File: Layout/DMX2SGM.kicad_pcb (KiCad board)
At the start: 2 copper layers, 66.4 x 90.9 mm, 38 parts, among them J1 AVR-ISP-6, J2 Conn_01x03, J3 Conn_01x03, J4 Conn_01x03, J5 Conn_01x03, SW1 BD09AV, U1 ATtiny1634, U2 485, U3 6N137, U4 REE-0505S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

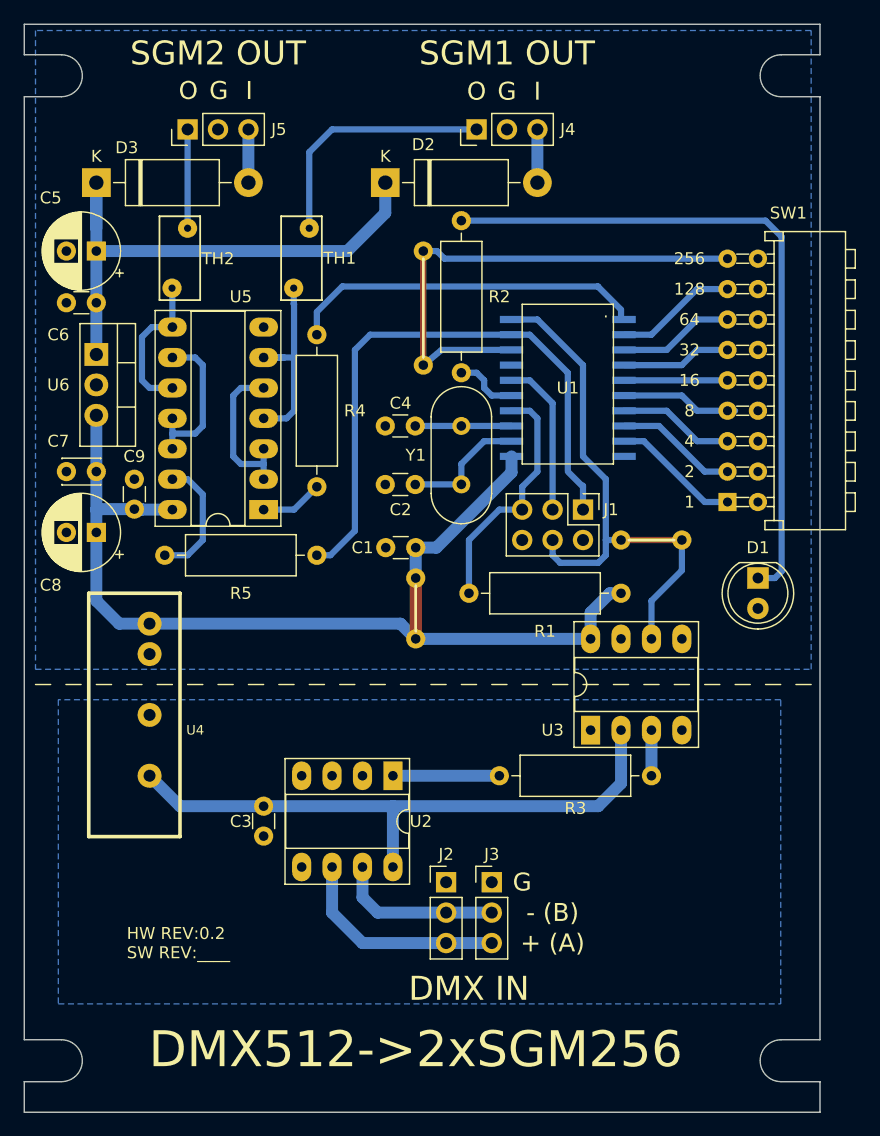
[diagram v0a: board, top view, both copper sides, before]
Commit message: Bugfixes & Cleanup
Code cleanup, Fixing a few bugs, General code optimations
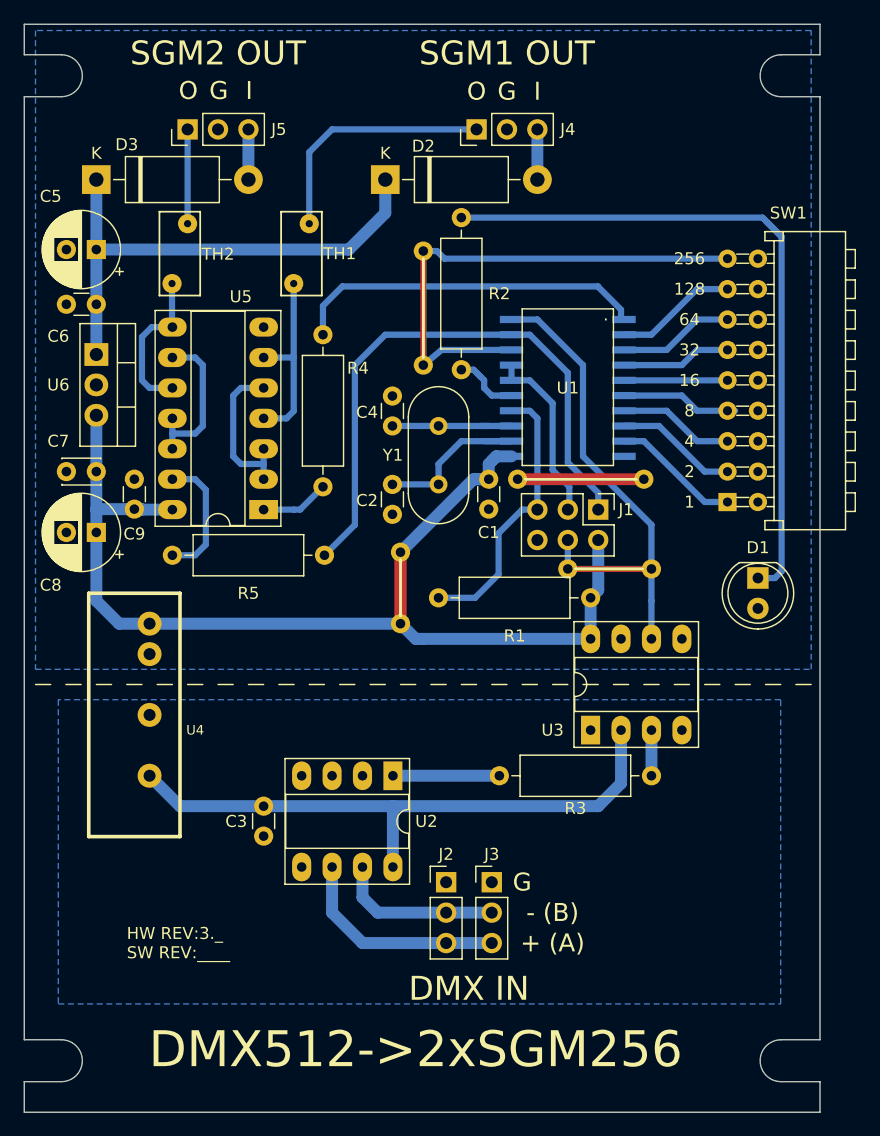
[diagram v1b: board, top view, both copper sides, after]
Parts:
- removed the REF** at (92.7, 101.0)
- removed the REF** at (109.9, 92.7)
- removed the REF** at (114.9, 92.7)
- added REF**: SolderWirePad_single_0-8mmDrill, Wire_Pads:SolderWirePad_single_0-8mmDrill, F.Cu at (101.2, 87.6)
- added REF**: SolderWirePad_single_0-8mmDrill, Wire_Pads:SolderWirePad_single_0-8mmDrill, F.Cu at (111.8, 87.6)
- added REF**: SolderWirePad_single_0-8mmDrill, Wire_Pads:SolderWirePad_single_0-8mmDrill, F.Cu at (91.4, 99.7)
- added REF**: SolderWirePad_single_0-8mmDrill, Wire_Pads:SolderWirePad_single_0-8mmDrill, F.Cu at (105.4, 95.1)
- added REF**: SolderWirePad_single_0-8mmDrill, Wire_Pads:SolderWirePad_single_0-8mmDrill, F.Cu at (112.4, 95.1)
- moved C1 8.36 mm to (98.8, 87.6), turned to 270 degrees
- moved R1 2.57 mm to (94.6, 97.5)
- moved C2 2.56 mm to (90.8, 90.6), turned to 90 degrees
- moved REF** 2.50 mm to (91.4, 93.7)
- moved C4 1.91 mm to (90.8, 83.2), turned to 90 degrees
- moved Y1 1.91 mm to (94.6, 83.2)
- moved J1 1.27 mm to (108.0, 90.2)
- moved R5 0.64 mm to (72.4, 94.0)
- moved R4 0.51 mm to (85.0, 88.3)
- moved TH1 0.38 mm to (83.8, 66.3)
- moved TH2 0.38 mm to (73.7, 66.3)
- moved D2 0.25 mm to (90.2, 62.6)
- moved D3 0.25 mm to (66.0, 62.6)
- moved R2 0.25 mm to (96.5, 65.8)
- moved C6 0.13 mm to (66.0, 73.0)
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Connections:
- J1 pad 2: (no net) -> +5VD
- U1 pad 17: (no net) -> ICSP_SCL
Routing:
- net GNDD: track 0.00 -> 10.5 mm
- net +5VD: track 89.2 -> 94.5 mm
- net DMX: track 47.4 -> 42.2 mm
- net Net-(C2-Pad2): track 9.90 -> 14.1 mm
- net +VSW: track 45.8 -> 42.8 mm
- net RESET: track 20.5 -> 23.4 mm
- net Net-(C4-Pad1): track 7.40 -> 9.94 mm
- net Net-(D1-Pad1): track 57.5 -> 59.5 mm
- net ICSP_SCL: track 13.1 -> 15.0 mm
- net Net-(TH1-Pad2): track 18.0 -> 16.6 mm
- net ICSP_MISO: track 50.7 -> 49.6 mm
- net Net-(D2-Pad2): track 5.08 -> 4.19 mm
- net Net-(R2-Pad2): track 5.35 -> 6.00 mm
- net Net-(R4-Pad1): track 5.23 -> 5.74 mm
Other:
- board text added: "HW REV:3._ SW REV:____"
- board text removed: "HW REV:0.2 SW REV:____"

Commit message: Fix random reboot, fix OBOE, improve layout
Fix MCU randomly rebooting.
Fix DMX address DIP switch off-by-one-error.
Modify PCB for easier device assembly.
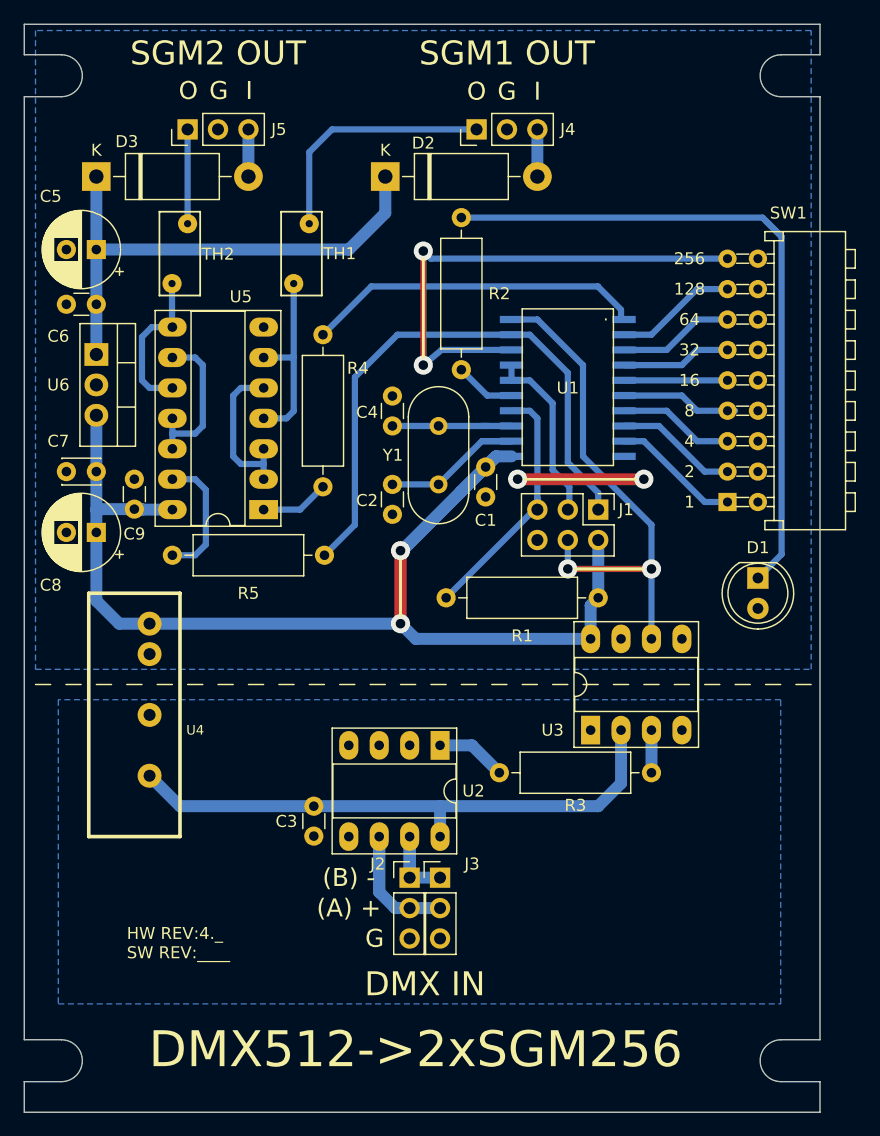
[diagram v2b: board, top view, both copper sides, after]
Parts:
- removed REF** (x8): SolderWirePad_single_0-8mmDrill, Wire_Pads:SolderWirePad_single_0-8mmDrill
- moved U2 4.69 mm to (94.7, 109.9)
- moved J3 4.33 mm to (94.7, 120.9)
- moved C3 4.19 mm to (84.2, 114.9)
- moved J2 3.07 mm to (92.2, 120.9)
- moved C1 1.05 mm to (98.6, 86.6)
- moved R1 0.64 mm to (95.2, 97.5)
- moved D2 0.25 mm to (90.2, 62.4)
- moved D3 0.25 mm to (66.0, 62.4)
- moved R3 0.25 mm to (112.4, 112.1)
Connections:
- J2 pad 1: GND -> Net-(J2-Pad1)
- J2 pad 3: Net-(J2-Pad3) -> GND
- J3 pad 1: GND -> Net-(J2-Pad1)
- J3 pad 3: Net-(J2-Pad3) -> GND
- U2 pad 6: Net-(J2-Pad3) -> Net-(J2-Pad2)
- U2 pad 7: Net-(J2-Pad2) -> Net-(J2-Pad1)
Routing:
- net Net-(J2-Pad3): track 18.2 -> 0.00 mm
- net +5VD: track 94.5 -> 106.3 mm, vias 0 -> 2
- net Net-(J2-Pad1): track 0.00 -> 9.27 mm
- net Net-(R3-Pad2): track 8.89 -> 5.90 mm
- net +5V: track 50.7 -> 48.2 mm
- net RESET: track 23.4 -> 21.7 mm
- net SGM_OUT_1: track 29.6 -> 28.2 mm
- net Net-(C2-Pad2): track 14.1 -> 13.1 mm
- net Net-(R2-Pad2): track 6.00 -> 5.08 mm
- net Net-(J2-Pad2): track 13.9 -> 14.8 mm
- net Net-(D1-Pad1): track 59.5 -> 58.6 mm
- net ICSP_MISO: track 49.6 -> 49.0 mm
- net /ADDRESS_8: track 43.5 -> 43.3 mm, vias 0 -> 2
- net GNDD: vias 0 -> 2
- net DMX: vias 0 -> 2
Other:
- board text added: "(A) +"
- board text added: "(B) -"
- board text added: "HW REV:4._ SW REV:____"
- board text removed: "+ (A)"
- board text removed: "- (B)"
- board text removed: "HW REV:3._ SW REV:____"
